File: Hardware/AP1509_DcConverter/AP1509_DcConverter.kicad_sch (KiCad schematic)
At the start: 13 parts, among them J2 01x02, J3 01x03, U1 AP1509

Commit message: Clean up schematics a bit
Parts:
- U1: symbol Angrywasp-IC:AP1509 -> Angrywasp.General:AP1509
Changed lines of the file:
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@@
 	)
 	(symbol
-		(lib_id "Angrywasp-IC:AP1509")
+		(lib_id "Angrywasp.General:AP1509")
 		(at 78.74 101.6 0)
 		(unit 1)

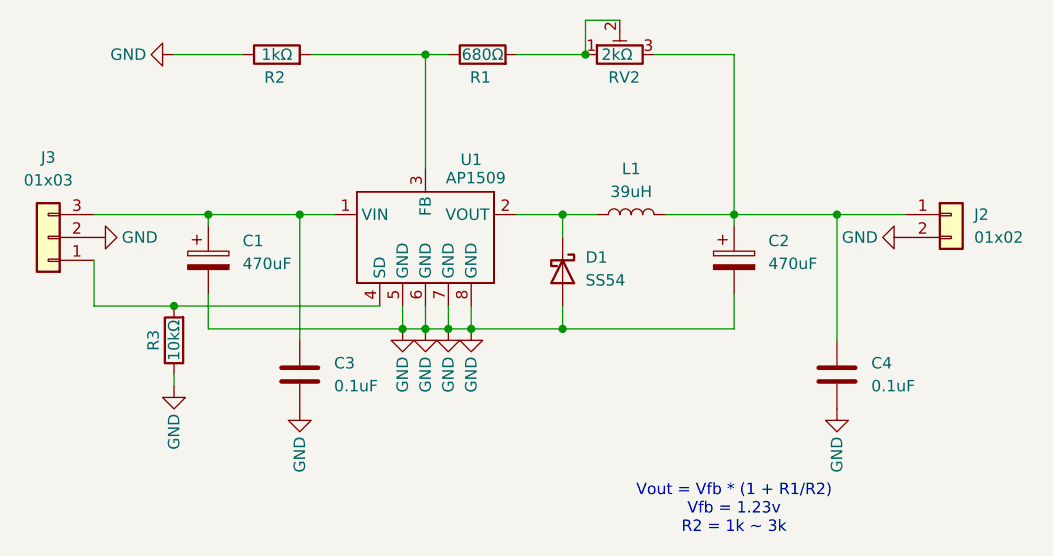
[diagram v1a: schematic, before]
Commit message: Hardware updates. Add Lr04 lora module datasheets
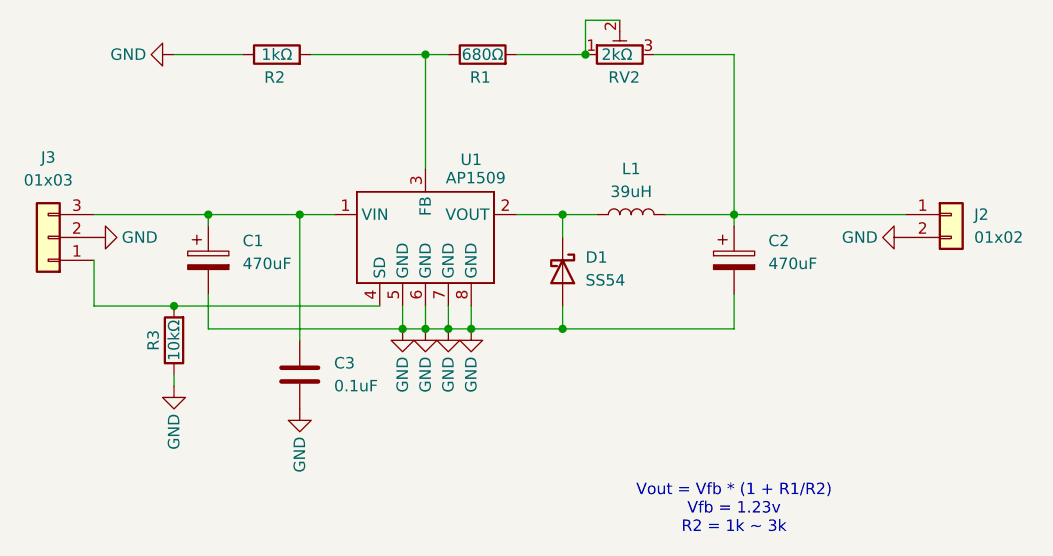
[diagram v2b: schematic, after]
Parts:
- removed C4: 0.1uF, Capacitor_SMD:C_0805_2012Metric_Pad1.18x1.45mm_HandSolder, symbol Device:C
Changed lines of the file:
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@@
-	)
-	(junction
-		(at 124.46 96.52)
-		(diameter 0)
-		(color 0 0 0 0)
 	)
 	(junction
@@
 	(wire
 		(pts
-			(xy 124.46 96.52) (xy 124.46 110.49)
-		)
-		(stroke
-			(width 0)
-			(type default)
-		)
-	)
-	(wire
-		(pts
 			(xy 50.8 115.57) (xy 50.8 114.3)
 		)
@@
 	(wire
 		(pts
-			(xy 113.03 96.52) (xy 124.46 96.52)
+			(xy 113.03 96.52) (xy 132.08 96.52)
 		)
 		(stroke
@@
 		(pts
 			(xy 78.74 78.74) (xy 78.74 91.44)
-		)
-		(stroke
-			(width 0)
-			(type default)
-		)
-	)
-	(wire
-		(pts
-			(xy 124.46 96.52) (xy 132.08 96.52)
 		)
 		(stroke
@@
 	)
 	(symbol
-		(lib_id "Device:C")
-		(at 124.46 114.3 0)
-		(unit 1)
-		(exclude_from_sim no)
-		(in_bom yes)
-		(on_board yes)
-		(dnp no)
-		(fields_autoplaced yes)
-		(property "Reference" "C4"
-			(at 128.27 113.0299 0)
-			(effects
-				(font
-					(size 1.27 1.27)
-				)
-				(justify left)
-			)
-		)
-		(property "Value" "0.1uF"
-			(at 128.27 115.5699 0)
-			(effects
-				(font
-					(size 1.27 1.27)
-				)
-				(justify left)
-			)
-		)
-		(property "Footprint" "Capacitor_SMD:C_0805_2012Metric_Pad1.18x1.45mm_HandSolder"
-			(at 125.4252 118.11 0)
-			(effects
-				(font
-					(size 1.27 1.27)
-				)
-				(hide yes)
-			)
-		)
-		(property "Datasheet" "~"
-			(at 124.46 114.3 0)
-			(effects
-				(font
-					(size 1.27 1.27)
-				)
-				(hide yes)
-			)
-		)
-		(property "Description" "Unpolarized capacitor"
-			(at 124.46 114.3 0)
-			(effects
-				(font
-					(size 1.27 1.27)
-				)
-				(hide yes)
-			)
-		)
-		(pin "1"
-		)
-		(pin "2"
-		)
-		(instances
-			(project "AP1509_DcConverter"
-				(path "/964c97b9-b585-4e56-86de-4c49dd6d519c"
-					(reference "C4")
-					(unit 1)
-				)
-			)
-		)
-	)
-	(symbol
 		(lib_id "Device:L")
 		(at 101.6 96.52 90)
@@
 					(unit 1)
 				)
-			)
-		)
-	)
-	(symbol
-		(lib_id "power:GND")
-		(at 124.46 118.11 0)
-		(unit 1)
-		(exclude_from_sim no)
-		(in_bom yes)
-		(on_board yes)
-		(dnp no)
-		(property "Reference" "#PWR010"
-			(at 124.46 124.46 0)
-			(effects
-				(font
-					(size 1.27 1.27)
-				)
-				(hide yes)
-			)
-		)
-		(property "Value" "GND"
-			(at 124.46 123.19 90)
-			(effects
-				(font
-					(size 1.27 1.27)
-				)
-			)
-		)
-		(property "Footprint" ""
-			(at 124.46 118.11 0)
-			(effects
-				(font
-					(size 1.27 1.27)
-				)
-				(hide yes)
-			)
-		)
-		(property "Datasheet" ""
-			(at 124.46 118.11 0)
-			(effects
-				(font
-					(size 1.27 1.27)
-				)
-				(hide yes)
-			)
-		)
-		(property "Description" "Power symbol creates a global label with name \"GND\" , ground"
-			(at 124.46 118.11 0)
-			(effects
-				(font
-					(size 1.27 1.27)
-				)
-				(hide yes)
-			)
-		)
-		(pin "1"
-		)
-		(instances
-			(project "AP1509_DcConverter"
-				(path "/964c97b9-b585-4e56-86de-4c49dd6d519c"
-					(reference "#PWR010")
-					(unit 1)
-				)
